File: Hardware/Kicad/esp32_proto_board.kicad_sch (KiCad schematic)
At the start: 12 parts, among them J13 Edge_Pads_Right_Top, J15 Edge_Pads_Right_Bottom, J23 Edge_Pads_Left_Top, J24 Edge_Pads_Left_Bottom

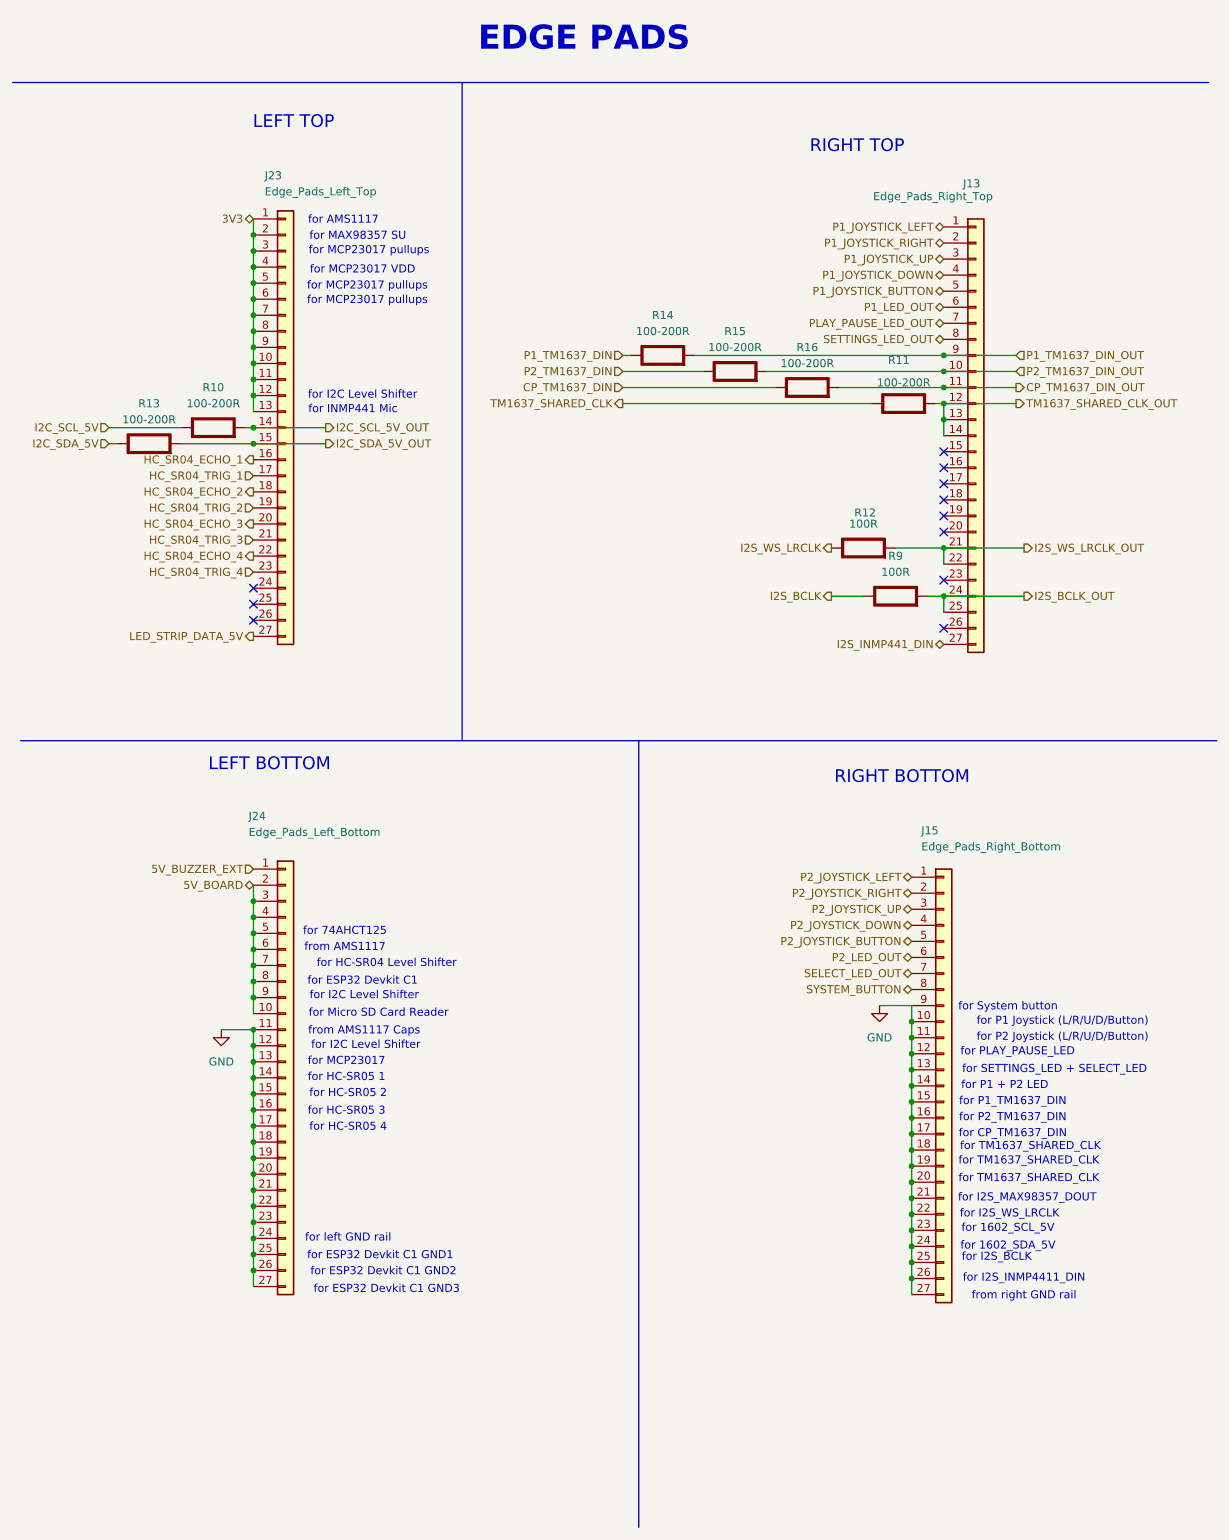
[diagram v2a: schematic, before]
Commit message: Added Kicad proto board
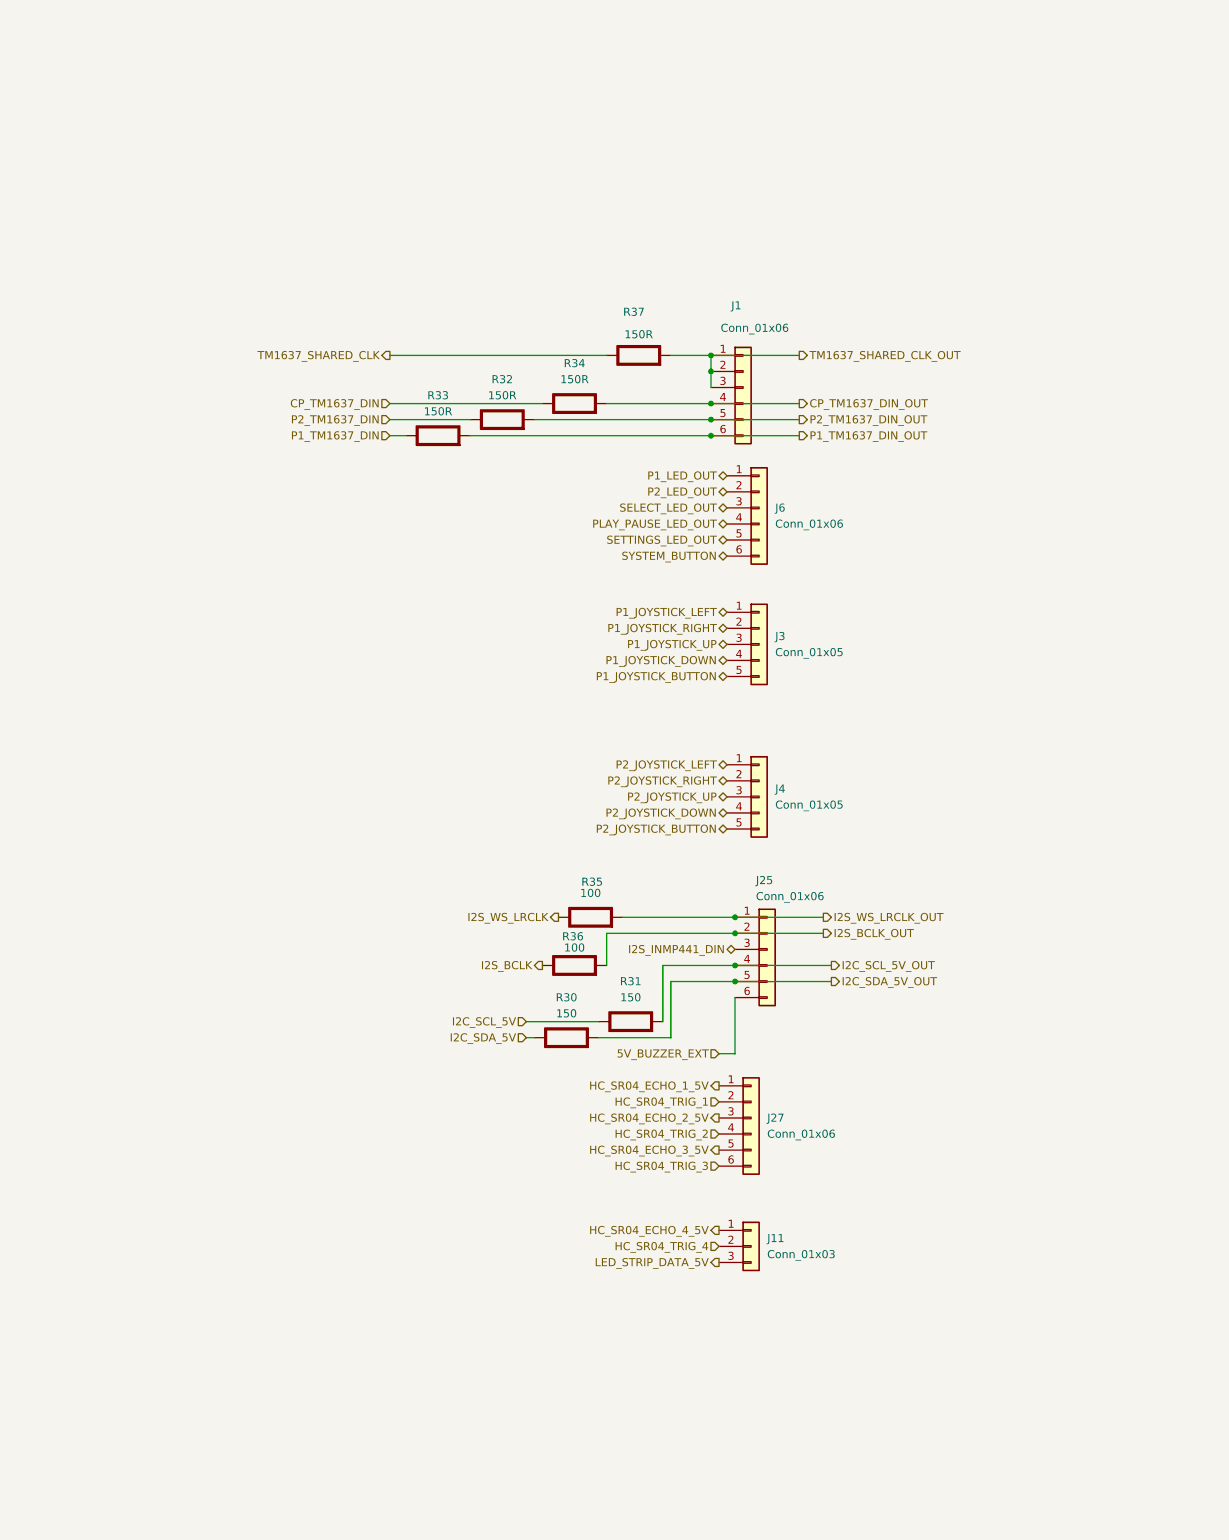
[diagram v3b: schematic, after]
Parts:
- removed J13: Edge_Pads_Right_Top, Connector_PinHeader_2.54mm:PinHeader_1x27_P2.54mm_Vertical_SMD_Pin1Left, symbol Connector_Generic:Conn_01x27
- removed J15: Edge_Pads_Right_Bottom, Connector_PinHeader_2.54mm:PinHeader_1x27_P2.54mm_Vertical_SMD_Pin1Left, symbol Connector_Generic:Conn_01x27
- removed J23: Edge_Pads_Left_Top, Connector_PinHeader_2.54mm:PinHeader_1x27_P2.54mm_Vertical_SMD_Pin1Left, symbol Connector_Generic:Conn_01x27
- removed J24: Edge_Pads_Left_Bottom, Connector_PinHeader_2.54mm:PinHeader_1x27_P2.54mm_Vertical_SMD_Pin1Left, symbol Connector_Generic:Conn_01x27
- removed R10, R11, R13, R14, R15, R16: 100-200R, Resistor_THT:R_Axial_DIN0204_L3.6mm_D1.6mm_P5.08mm_Horizontal, symbol PCM_Elektuur:R
- removed R12, R9: 100R, Resistor_THT:R_Axial_DIN0204_L3.6mm_D1.6mm_P5.08mm_Horizontal, symbol PCM_Elektuur:R
- added J1, J25, J27, J6: Conn_01x06, Connector_JST:JST_XH_B6B-XH-A_1x06_P2.50mm_Vertical, symbol PCM_4ms_Connector:Conn_01x06
- added J11: Conn_01x03, Connector_JST:JST_XH_B3B-XH-A_1x03_P2.50mm_Vertical, symbol PCM_4ms_Connector:Conn_01x03
- added J3, J4: Conn_01x05, Connector_JST:JST_XH_B5B-XH-A_1x05_P2.50mm_Vertical, symbol Connector_Generic:Conn_01x05
- added R30, R31: 150, PCM_Resistor_SMD_AKL:R_0805_2012Metric_Pad1.20x1.40mm_HandSolder, symbol PCM_Elektuur:R
- added R32, R33, R34, R37: 150R, PCM_Resistor_SMD_AKL:R_0805_2012Metric_Pad1.20x1.40mm_HandSolder, symbol PCM_Elektuur:R
- added R35, R36: 100, PCM_Resistor_SMD_AKL:R_0805_2012Metric_Pad1.20x1.40mm_HandSolder, symbol PCM_Elektuur:R
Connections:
- net 5V_BUZZER_EXT: now also J25.6 (Pin_6)
- net CP_TM1637_DIN: now also R34.1 (+)
- net CP_TM1637_DIN_OUT: now also J1.4 (Pin_4), R34.2 (-)
- net HC_SR04_TRIG_1: now also J27.2 (Pin_2)
- net HC_SR04_TRIG_2: now also J27.4 (Pin_4)
- net HC_SR04_TRIG_3: now also J27.6 (Pin_6)
- net HC_SR04_TRIG_4: now also J11.2 (Pin_2)
- net I2C_SCL_5V: now also R31.1 (+)
- net I2C_SCL_5V_OUT: now also J25.4 (Pin_4), R31.2 (-)
- net I2C_SDA_5V: now also R30.1 (+)
- net I2C_SDA_5V_OUT: now also J25.5 (Pin_5), R30.2 (-)
- net I2S_BCLK: now also R36.1 (+)
- net I2S_BCLK_OUT: now also J25.2 (Pin_2), R36.2 (-)
- net I2S_INMP441_DIN: now also J25.3 (Pin_3)
- net I2S_WS_LRCLK: now also R35.1 (+)
- net I2S_WS_LRCLK_OUT: now also J25.1 (Pin_1), R35.2 (-)
- net LED_STRIP_DATA_5V: now also J11.3 (Pin_3)
- net P1_JOYSTICK_BUTTON: now also J3.5 (Pin_5)
- net P1_JOYSTICK_DOWN: now also J3.4 (Pin_4)
- net P1_JOYSTICK_LEFT: now also J3.1 (Pin_1)
- net P1_JOYSTICK_RIGHT: now also J3.2 (Pin_2)
- net P1_JOYSTICK_UP: now also J3.3 (Pin_3)
- net P1_LED_OUT: now also J6.1 (Pin_1)
- net P1_TM1637_DIN: now also R33.1 (+)
- net P1_TM1637_DIN_OUT: now also J1.6 (Pin_6), R33.2 (-)
- net P2_JOYSTICK_BUTTON: now also J4.5 (Pin_5)
- net P2_JOYSTICK_DOWN: now also J4.4 (Pin_4)
- net P2_JOYSTICK_LEFT: now also J4.1 (Pin_1)
- net P2_JOYSTICK_RIGHT: now also J4.2 (Pin_2)
- net P2_JOYSTICK_UP: now also J4.3 (Pin_3)
- net P2_LED_OUT: now also J6.2 (Pin_2)
- net P2_TM1637_DIN: now also R32.1 (+)
- net P2_TM1637_DIN_OUT: now also J1.5 (Pin_5), R32.2 (-)
- net PLAY_PAUSE_LED_OUT: now also J6.4 (Pin_4)
- net SELECT_LED_OUT: now also J6.3 (Pin_3)
- net SETTINGS_LED_OUT: now also J6.5 (Pin_5)
- net SYSTEM_BUTTON: now also J6.6 (Pin_6)
- net TM1637_SHARED_CLK: now also R37.1 (+)
- net TM1637_SHARED_CLK_OUT: now also J1.1 (Pin_1), J1.2 (Pin_2), J1.3 (Pin_3), R37.2 (-)
- new net HC_SR04_ECHO_1_5V: J27.1 (Pin_1)
- new net HC_SR04_ECHO_2_5V: J27.3 (Pin_3)
- new net HC_SR04_ECHO_3_5V: J27.5 (Pin_5)
- new net HC_SR04_ECHO_4_5V: J11.1 (Pin_1)
- no-connect marks 11 -> 0
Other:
- note removed: "EDGE PADS"
- note removed: "LEFT BOTTOM"
- note removed: "LEFT TOP"
- note removed: "RIGHT BOTTOM"
- note removed: "RIGHT TOP"
- note removed: "for 1602_SCL_5V"
- note removed: "for 1602_SDA_5V"
- note removed: "for 74AHCT125"
- note removed: "for AMS1117"
- note removed: "for CP_TM1637_DIN"
- note removed: "for ESP32 Devkit C1"
- note removed: "for ESP32 Devkit C1 GND1"
- note removed: "for ESP32 Devkit C1 GND2"
- note removed: "for ESP32 Devkit C1 GND3"
- note removed: "for HC-SR04 Level Shifter"
- note removed: "for HC-SR05 1"
- note removed: "for HC-SR05 2"
- note removed: "for HC-SR05 3"
- note removed: "for HC-SR05 4"
- note removed: "for I2C Level Shifter"
- note removed: "for I2S_BCLK"
- note removed: "for I2S_INMP4411_DIN"
- note removed: "for I2S_MAX98357_DOUT"
- note removed: "for I2S_WS_LRCLK"
- note removed: "for INMP441 Mic"
- note removed: "for MAX98357 SU"
- note removed: "for MCP23017"
- note removed: "for MCP23017 VDD"
- note removed: "for MCP23017 pullups"
- note removed: "for Micro SD Card Reader"
- note removed: "for P1 + P2 LED"
- note removed: "for P1 Joystick (L/R/U/D/Button)"
- note removed: "for P1_TM1637_DIN"
- note removed: "for P2 Joystick (L/R/U/D/Button)"
- note removed: "for P2_TM1637_DIN"
- note removed: "for PLAY_PAUSE_LED"
- note removed: "for SETTINGS_LED + SELECT_LED"
- note removed: "for System button"
- note removed: "for TM1637_SHARED_CLK"
- note removed: "for left GND rail"
- note removed: "from AMS1117"
- note removed: "from AMS1117 Caps"
- note removed: "from right GND rail"
